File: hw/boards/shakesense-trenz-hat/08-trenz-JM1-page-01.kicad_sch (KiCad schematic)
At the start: 1 part, among them J80 LSHM-150-04.0-L-DV-A-S-K-TR

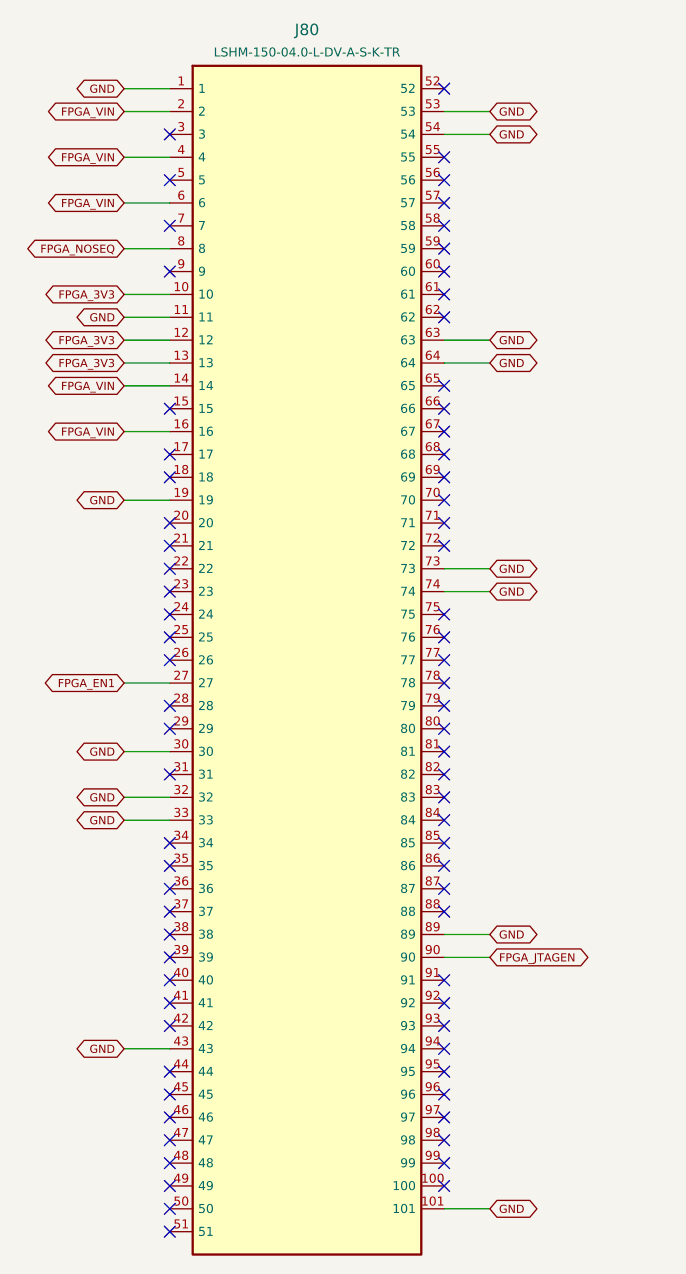
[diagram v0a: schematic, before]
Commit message: Expose Trenz GPIOs on the Pi-outline HDI sensor HAT
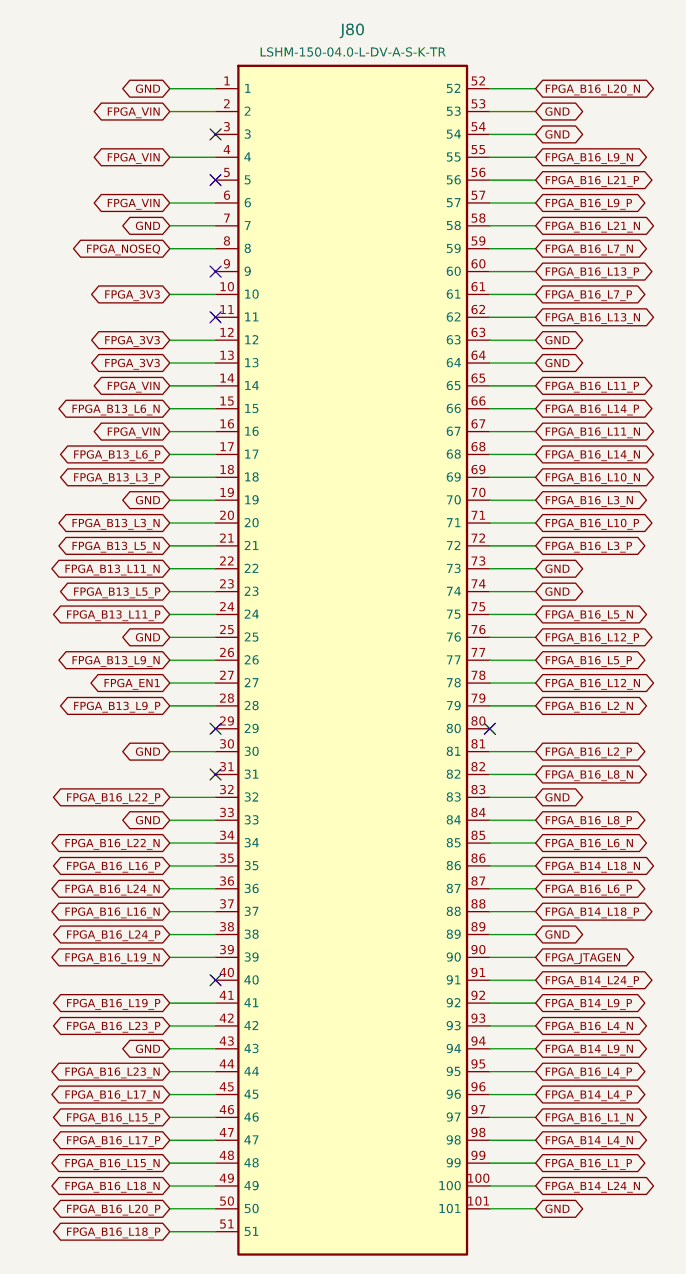
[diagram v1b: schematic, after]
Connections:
- net GND: now also J80.25, J80.7, J80.83; no longer J80.11, J80.32
- net FPGA_B14_L24_N: now reaches J80.100
- net FPGA_B13_L6_N: now reaches J80.15
- net FPGA_B13_L6_P: now reaches J80.17
- net FPGA_B13_L3_P: now reaches J80.18
- net FPGA_B13_L3_N: now reaches J80.20
- net FPGA_B13_L5_N: now reaches J80.21
- net FPGA_B13_L11_N: now reaches J80.22
- net FPGA_B13_L5_P: now reaches J80.23
- net FPGA_B13_L11_P: now reaches J80.24
- net FPGA_B13_L9_N: now reaches J80.26
- net FPGA_B13_L9_P: now reaches J80.28
- net FPGA_B16_L22_N: now reaches J80.34
- net FPGA_B16_L16_P: now reaches J80.35
- net FPGA_B16_L24_N: now reaches J80.36
- net FPGA_B16_L16_N: now reaches J80.37
- net FPGA_B16_L24_P: now reaches J80.38
- net FPGA_B16_L19_N: now reaches J80.39
- net FPGA_B16_L19_P: now reaches J80.41
- net FPGA_B16_L23_P: now reaches J80.42
- net FPGA_B16_L23_N: now reaches J80.44
- net FPGA_B16_L17_N: now reaches J80.45
- net FPGA_B16_L15_P: now reaches J80.46
- net FPGA_B16_L17_P: now reaches J80.47
- net FPGA_B16_L15_N: now reaches J80.48
- net FPGA_B16_L18_N: now reaches J80.49
- net FPGA_B16_L20_P: now reaches J80.50
- net FPGA_B16_L18_P: now reaches J80.51
- net FPGA_B16_L20_N: now reaches J80.52
- net FPGA_B16_L9_N: now reaches J80.55
- net FPGA_B16_L21_P: now reaches J80.56
- net FPGA_B16_L9_P: now reaches J80.57
- net FPGA_B16_L21_N: now reaches J80.58
- net FPGA_B16_L7_N: now reaches J80.59
- net FPGA_B16_L13_P: now reaches J80.60
- net FPGA_B16_L7_P: now reaches J80.61
- net FPGA_B16_L13_N: now reaches J80.62
- net FPGA_B16_L11_P: now reaches J80.65
- net FPGA_B16_L14_P: now reaches J80.66
- net FPGA_B16_L11_N: now reaches J80.67
- net FPGA_B16_L14_N: now reaches J80.68
- net FPGA_B16_L10_N: now reaches J80.69
- net FPGA_B16_L3_N: now reaches J80.70
- net FPGA_B16_L10_P: now reaches J80.71
- net FPGA_B16_L3_P: now reaches J80.72
- net FPGA_B16_L5_N: now reaches J80.75
- net FPGA_B16_L12_P: now reaches J80.76
- net FPGA_B16_L5_P: now reaches J80.77
- net FPGA_B16_L12_N: now reaches J80.78
- net FPGA_B16_L2_N: now reaches J80.79
- net FPGA_B16_L2_P: now reaches J80.81
- net FPGA_B16_L8_N: now reaches J80.82
- net FPGA_B16_L8_P: now reaches J80.84
- net FPGA_B16_L6_N: now reaches J80.85
- net FPGA_B14_L18_N: now reaches J80.86
- net FPGA_B16_L6_P: now reaches J80.87
- net FPGA_B14_L18_P: now reaches J80.88
- net FPGA_B14_L24_P: now reaches J80.91
- net FPGA_B14_L9_P: now reaches J80.92
- net FPGA_B16_L4_N: now reaches J80.93
- net FPGA_B14_L9_N: now reaches J80.94
- net FPGA_B16_L4_P: now reaches J80.95
- net FPGA_B14_L4_P: now reaches J80.96
- net FPGA_B16_L1_N: now reaches J80.97
- net FPGA_B14_L4_N: now reaches J80.98
- net FPGA_B16_L1_P: now reaches J80.99
- new net FPGA_B16_L22_P: J80.32
- no-connect marks 75 -> 8
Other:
- title: shakesense-trenz-hat / 08-trenz-JM1-page-01 -> ShakeSense T1 / 08-trenz-JM1-page-01
- moved on the sheet: J80

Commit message: Implement internal Pi FPGA link and remove ribbon expansion
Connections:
- net FPGA_B13_L11_N: no longer names the net of J80.22
- net FPGA_B13_L11_P: no longer names the net of J80.24
- net FPGA_B13_L3_N: no longer names the net of J80.20
- net FPGA_B13_L3_P: no longer names the net of J80.18
- net FPGA_B13_L5_N: no longer names the net of J80.21
- net FPGA_B13_L5_P: no longer names the net of J80.23
- net FPGA_B13_L6_N: no longer names the net of J80.15
- net FPGA_B13_L6_P: no longer names the net of J80.17
- net FPGA_B13_L9_N: no longer names the net of J80.26
- net FPGA_B13_L9_P: no longer names the net of J80.28
- net FPGA_B14_L18_N: no longer names the net of J80.86
- net FPGA_B14_L18_P: no longer names the net of J80.88
- net FPGA_B14_L24_N: no longer names the net of J80.100
- net FPGA_B14_L24_P: no longer names the net of J80.91
- net FPGA_B14_L4_N: no longer names the net of J80.98
- net FPGA_B14_L4_P: no longer names the net of J80.96
- net FPGA_B14_L9_N: no longer names the net of J80.94
- net FPGA_B14_L9_P: no longer names the net of J80.92
- net FPGA_B16_L10_N: no longer names the net of J80.69
- net FPGA_B16_L10_P: no longer names the net of J80.71
- net FPGA_B16_L11_N: no longer names the net of J80.67
- net FPGA_B16_L11_P: no longer names the net of J80.65
- net FPGA_B16_L12_N: no longer names the net of J80.78
- net FPGA_B16_L12_P: no longer names the net of J80.76
- net FPGA_B16_L13_N: no longer names the net of J80.62
- net FPGA_B16_L13_P: no longer names the net of J80.60
- net FPGA_B16_L14_N: no longer names the net of J80.68
- net FPGA_B16_L14_P: no longer names the net of J80.66
- net FPGA_B16_L15_N: no longer names the net of J80.48
- net FPGA_B16_L15_P: no longer names the net of J80.46
- net FPGA_B16_L16_N: no longer names the net of J80.37
- net FPGA_B16_L16_P: no longer names the net of J80.35
- net FPGA_B16_L17_N: no longer names the net of J80.45
- net FPGA_B16_L17_P: no longer names the net of J80.47
- net FPGA_B16_L18_N: no longer names the net of J80.49
- net FPGA_B16_L18_P: no longer names the net of J80.51
- net FPGA_B16_L19_N: no longer names the net of J80.39
- net FPGA_B16_L19_P: no longer names the net of J80.41
- net FPGA_B16_L1_N: no longer names the net of J80.97
- net FPGA_B16_L1_P: no longer names the net of J80.99
- net FPGA_B16_L20_N: no longer names the net of J80.52
- net FPGA_B16_L20_P: no longer names the net of J80.50
- net FPGA_B16_L21_N: no longer names the net of J80.58
- net FPGA_B16_L21_P: no longer names the net of J80.56
- net FPGA_B16_L22_N: no longer names the net of J80.34
- net FPGA_B16_L22_P: no longer names the net of J80.32
- net FPGA_B16_L23_N: no longer names the net of J80.44
- net FPGA_B16_L23_P: no longer names the net of J80.42
- net FPGA_B16_L24_N: no longer names the net of J80.36
- net FPGA_B16_L24_P: no longer names the net of J80.38
- net FPGA_B16_L2_N: no longer names the net of J80.79
- net FPGA_B16_L2_P: no longer names the net of J80.81
- net FPGA_B16_L3_N: no longer names the net of J80.70
- net FPGA_B16_L3_P: no longer names the net of J80.72
- net FPGA_B16_L4_N: no longer names the net of J80.93
- net FPGA_B16_L4_P: no longer names the net of J80.95
- net FPGA_B16_L5_N: no longer names the net of J80.75
- net FPGA_B16_L5_P: no longer names the net of J80.77
- net FPGA_B16_L6_N: no longer names the net of J80.85
- net FPGA_B16_L6_P: no longer names the net of J80.87
- net FPGA_B16_L7_N: no longer names the net of J80.59
- net FPGA_B16_L7_P: no longer names the net of J80.61
- net FPGA_B16_L8_N: no longer names the net of J80.82
- net FPGA_B16_L8_P: no longer names the net of J80.84
- net FPGA_B16_L9_N: no longer names the net of J80.55
- net FPGA_B16_L9_P: no longer names the net of J80.57
- no-connect marks 8 -> 74
